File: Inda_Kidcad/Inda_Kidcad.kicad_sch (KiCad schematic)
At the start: 66 parts, among them J1 SERIALWIRE, J10 Conn_01x03_Pin, J15 Conn_01x02_Pin, J16 Conn_01x01_Pin, J17 Conn_01x01_Pin, J19 Conn_01x02_Pin, J2 LIPO, J20 Conn_01x02_Pin, J21 Conn_01x03_Pin, J22 Conn_01x03_Pin, J23 Conn_01x02_Pin, J24 Conn_01x02_Pin, J25 Conn_01x02_Pin, J3 BRIDGE, J8 Conn_01x02_Pin, J9 Conn_01x02_Pin, Q5 AO3401A, Q6 AO3401A, SW1 SW_Push, SW2 SW_Push, SW3 SW_Push_SPDT, SW4 SW_Push, SW5 SW_Push, SW6 SW_Push, U1 STM32f103C8t6, U12 vs1838, Y2 8Mhz

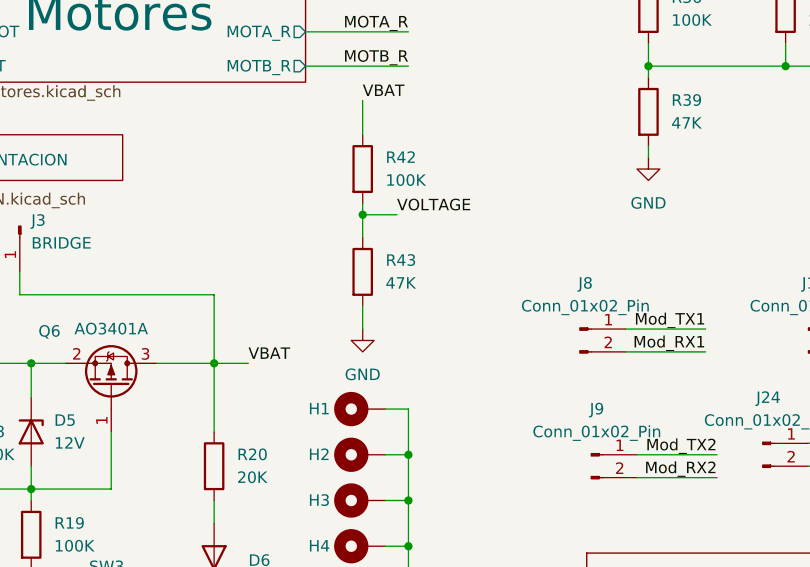
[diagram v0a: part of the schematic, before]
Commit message: sensores probados y rc5 funcionando
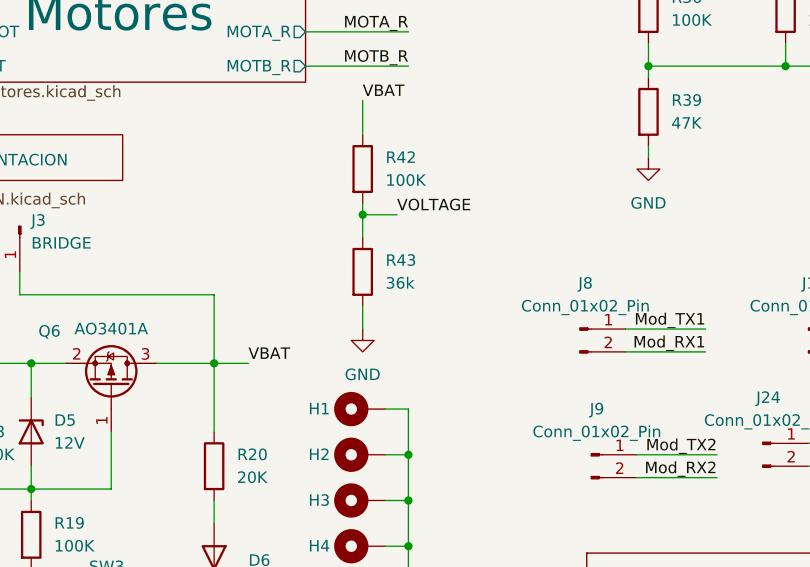
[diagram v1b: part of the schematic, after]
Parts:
- R43: value 47K -> 36k
